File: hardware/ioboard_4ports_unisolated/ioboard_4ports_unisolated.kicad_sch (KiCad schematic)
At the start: 54 parts

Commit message: Finish IO-Board updates
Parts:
- C1, C2, C3, C4: value (none) -> 100nF; footprint (none) -> Capacitor_SMD:C_0603_1608Metric
- H1, H2, H3, H4: value (none) -> MountingHole; footprint (none) -> MountingHole:MountingHole_3.2mm_M3
- J1: value (none) -> Conn_02x06_Odd_Even; footprint (none) -> Connector_PinHeader_2.54mm:PinHeader_2x06_P2.54mm_Vertical
- J10, J2, J4, J8: value (none) -> XLR3; footprint (none) -> Connector_Audio:Jack_XLR_Neutrik_NC3FAAH_Horizontal
- J11, J3, J5, J9: value (none) -> XLR3; footprint (none) -> NC3FD-H:Jack_XLR_Neutrik_NC3FD-H_Horizontal
- J12, J13, J6, J7: value (none) -> Conn_01x03; footprint (none) -> Connector_PinHeader_2.54mm:PinHeader_1x03_P2.54mm_Vertical
- R1, R11, R12, R17, R18, R2, R7, R8: value (none) -> 680R; footprint (none) -> Resistor_SMD:R_0603_1608Metric_Pad0.98x0.95mm_HandSolder
- R10, R14, R20, R22, R24, R27, R28, R9: value (none) -> 0R-DO_NOT_MOUNT; footprint (none) -> Resistor_SMD:R_0805_2012Metric_Pad1.20x1.40mm_HandSolder
- R13, R19, R21, R23, R25, R26, R3, R4: value (none) -> 0R; footprint (none) -> Resistor_SMD:R_0805_2012Metric_Pad1.20x1.40mm_HandSolder
- R15, R16, R5, R6: value (none) -> 120R; footprint (none) -> Resistor_SMD:R_0603_1608Metric_Pad0.98x0.95mm_HandSolder
- U1: value (none) -> M24C64-RMN6TP; footprint (none) -> Package_SO:SOIC-8_3.9x4.9mm_P1.27mm; LCSC C7562 -> C79988
- U2, U3, U4, U5: value (none) -> SP3485EN; footprint (none) -> Package_SO:SOIC-8_3.9x4.9mm_P1.27mm
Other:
- note added: "I2C EEPROM for board identification and configuration storage"
- note removed: "I2C EEPROM for board identification"

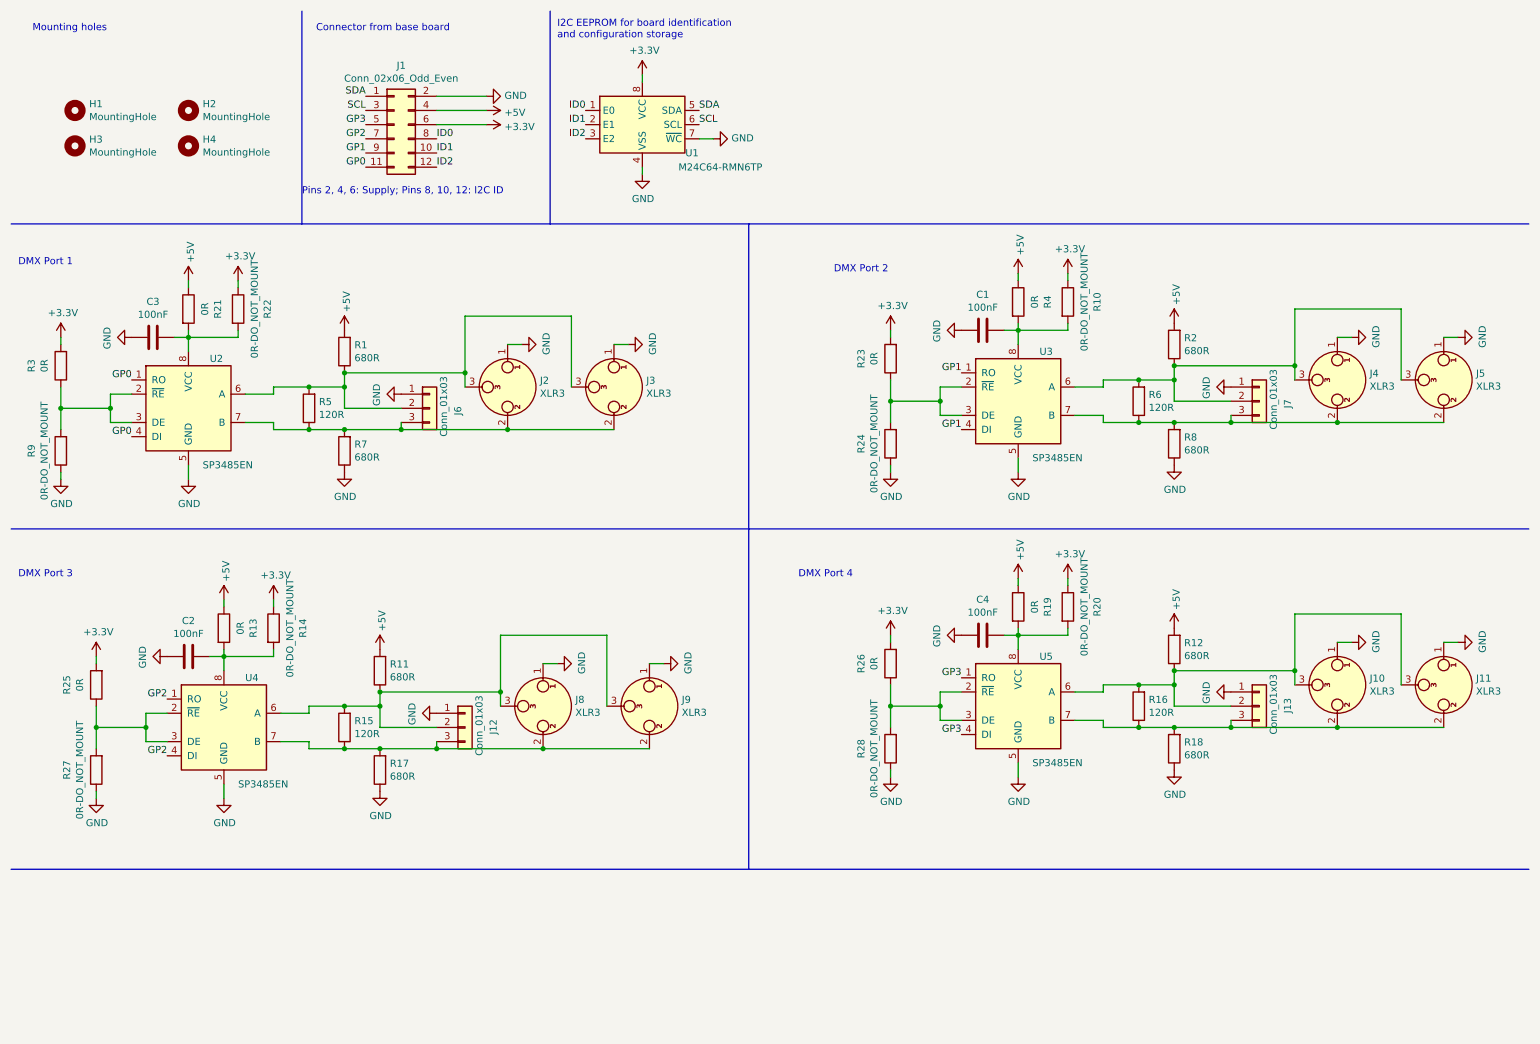
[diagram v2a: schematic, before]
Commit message: Add RJ45 jack to ioboard_4ports_unisolated as well
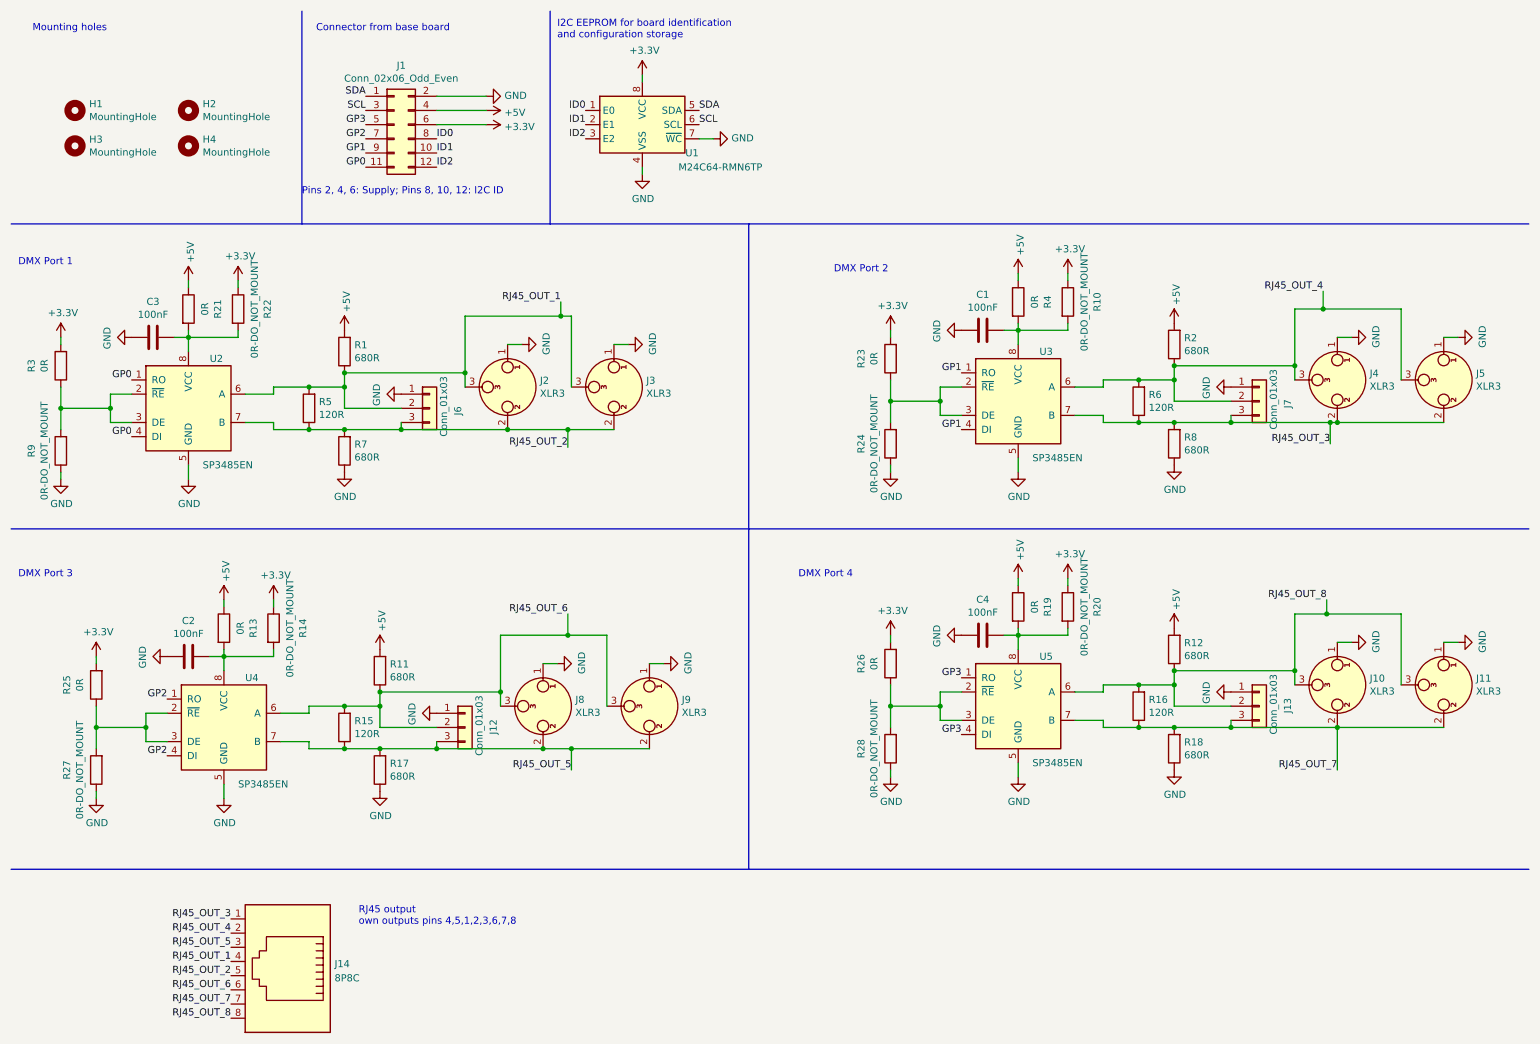
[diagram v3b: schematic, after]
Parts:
- added J14: 8P8C, RJ45_Sparkfun:RJ45_Sparkfun, symbol Connector:8P8C
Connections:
- net RJ45_OUT_1: now reaches J2.3, J3.3, J6.2 (Pin_2), R1.1, R5.2, U2.6 (A)
- net RJ45_OUT_1: now also J14.4
- net RJ45_OUT_2: now reaches J2.2, J3.2, J6.3 (Pin_3), R5.1, R7.2, U2.7 (B)
- net RJ45_OUT_2: now also J14.5
- net RJ45_OUT_4: now reaches J4.3, J5.3, J7.2 (Pin_2), R2.1, R6.2, U3.6 (A)
- net RJ45_OUT_4: now also J14.2
- net RJ45_OUT_3: now reaches J4.2, J5.2, J7.3 (Pin_3), R6.1, R8.2, U3.7 (B)
- net RJ45_OUT_3: now also J14.1
- net RJ45_OUT_5: now reaches J12.3 (Pin_3), J8.2, J9.2, R15.1, R17.2, U4.7 (B)
- net RJ45_OUT_5: now also J14.3
- net RJ45_OUT_6: now reaches J12.2 (Pin_2), J8.3, J9.3, R11.1, R15.2, U4.6 (A)
- net RJ45_OUT_6: now also J14.6
- net RJ45_OUT_7: now reaches J10.2, J11.2, J13.3 (Pin_3), R16.1, R18.2, U5.7 (B)
- net RJ45_OUT_7: now also J14.7
- net RJ45_OUT_8: now reaches J10.3, J11.3, J13.2 (Pin_2), R12.1, R16.2, U5.6 (A)
- net RJ45_OUT_8: now also J14.8
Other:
- note added: "RJ45 output own outputs pins 4,5,1,2,3,6,7,8"

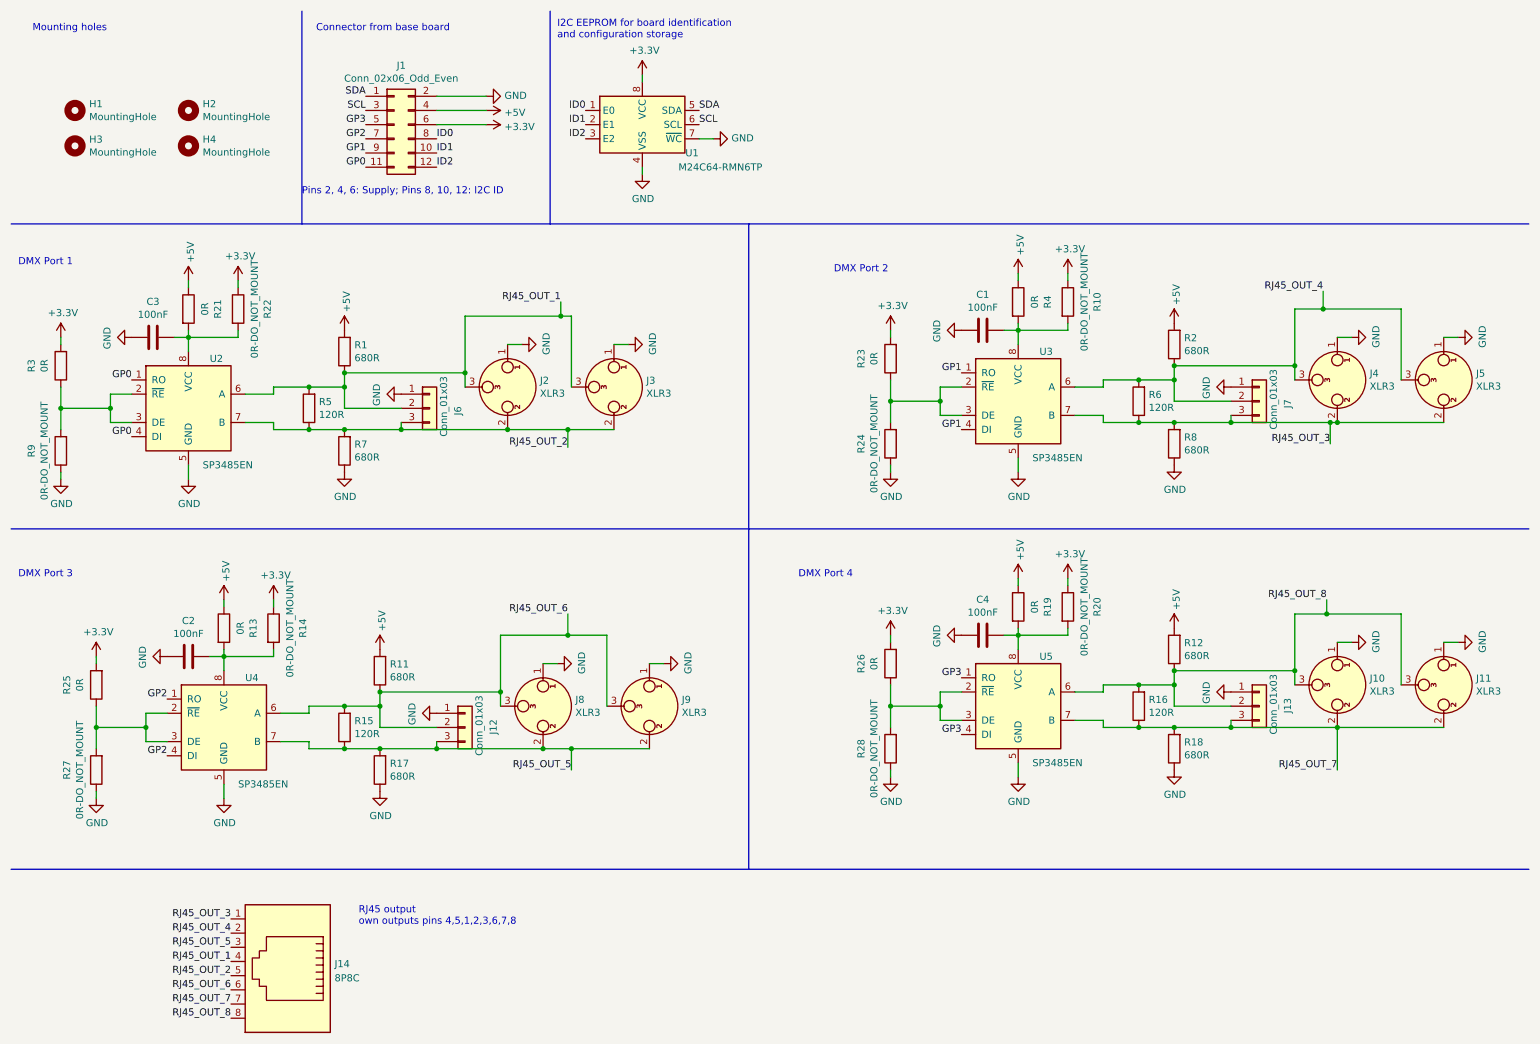
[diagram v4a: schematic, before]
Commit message: Update ioboards to KiCad 8, add OpenHardware logo
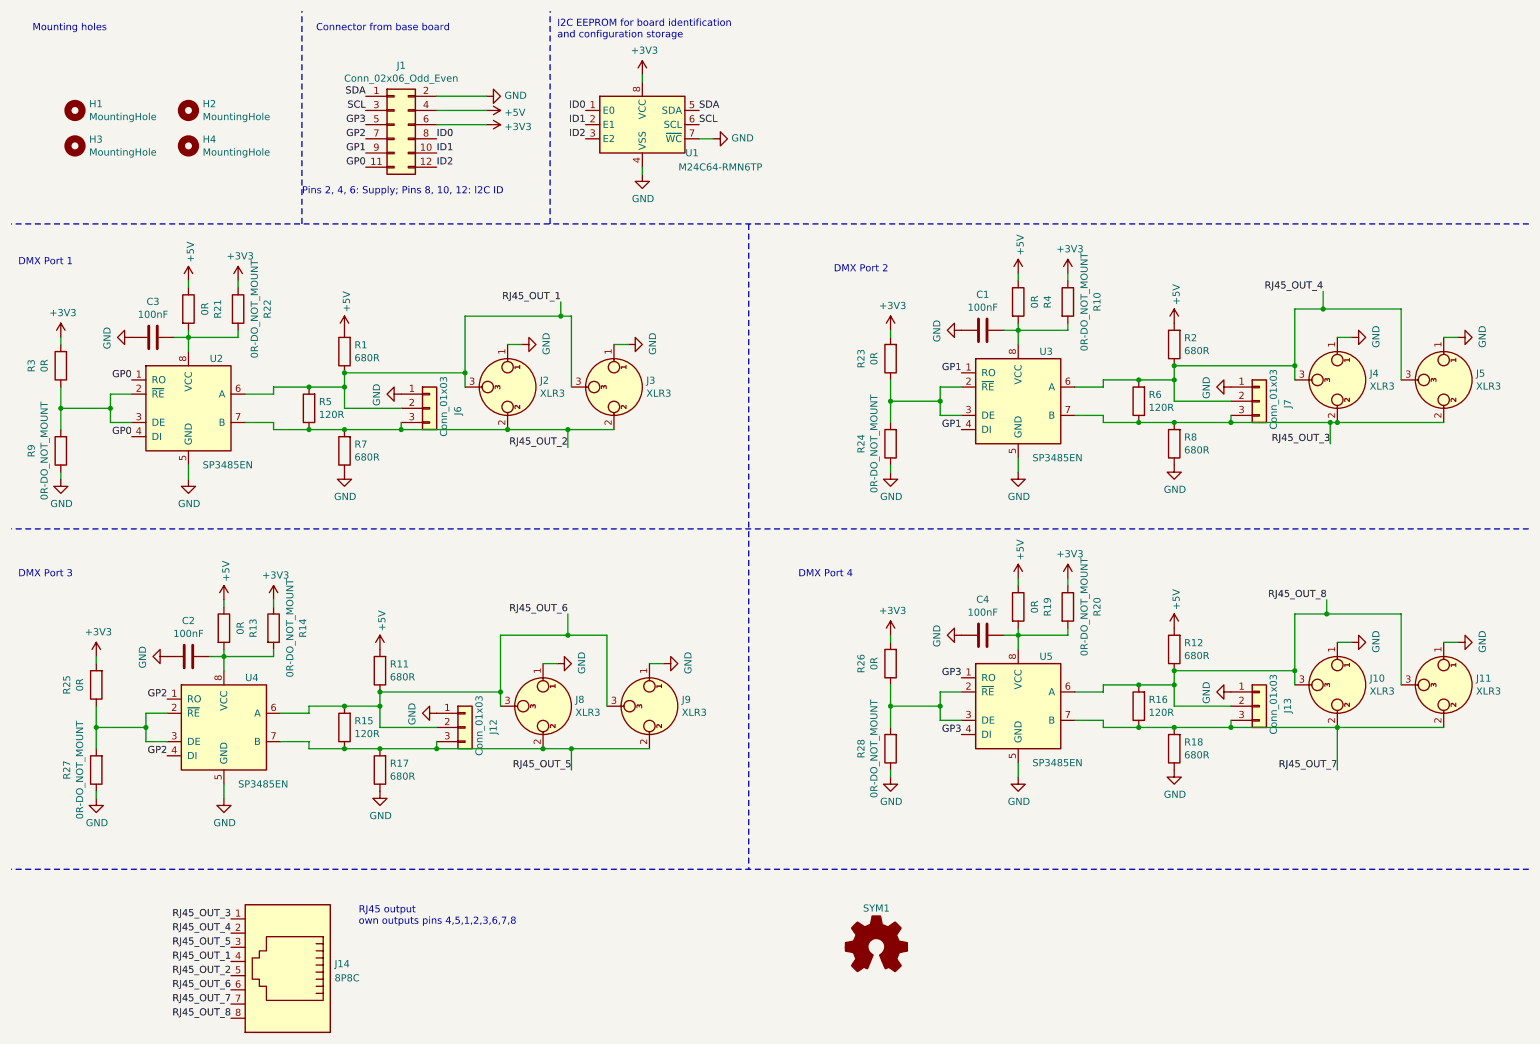
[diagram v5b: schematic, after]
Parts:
- added SYM1: Logo_Open_Hardware_Small, Symbol:OSHW-Logo2_7.3x6mm_SilkScreen, symbol Graphic:Logo_Open_Hardware_Small
